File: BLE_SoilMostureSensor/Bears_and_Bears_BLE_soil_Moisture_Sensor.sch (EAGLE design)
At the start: 51 parts, among them Q1 2N3904, U2 EFR32BG13, X1 20317

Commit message: fixing antenna
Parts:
- removed FID1, FID2: FIDUCIAL"", microbuilder:FIDUCIAL""
- removed TP6: TEST-POINT3, SparkFun-Connectors:TEST-POINT3
- added R11: 4.7k, SparkFun-Resistors:4.7KOHM-0603-1/10W-1%
- added Y1: (no value), Crystal_SMD_1.2x0.6:32.768KHZ_LOW_FREQ_CRYSTAL
- L1: value L100 -> 33nH/±5%/500mA
- L2, L4: value 1.9NH -> 3.9NH
- U$3: value 38.4MHZ_CRYSTAL -> (none)
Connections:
- removed net N$52: X1.GNDDETECT
- removed net N$7: TP6.1
- removed net N$8: TP5.1
- new net GND_DETECT: R11.1, U2.PD14, X1.GNDDETECT
- new net HFXTAL_N: U$3.1, U2.HFXTAL_N
- new net HFXTAL_P: U$3.2, U2.HFXTAL_P
- new net LFXTAL_N: U2.PB14, Y1.1
- new net LFXTAL_P: U2.PB15, Y1.2
- new net N$10: U2.PF5
- new net N$11: U2.PF6
- new net N$12: U2.PF7
- new net N$16: U2.PA1
- new net N$17: U2.PA2
- new net N$18: U2.PA3
- new net N$19: U2.PA4
- new net N$2: U2.GND, U2.PAVSS, U2.RFVSS, U2.VREGVSS
- new net N$20: U2.PA5
- new net N$9: U2.PF4
- net DECOUPLE: now also U2.DECOUPLE; no longer U2.IOVDD
- net GND: now also U$3.GND, U2.2G4RF_ION
- net IOP: now also U2.2G4RF_IOP
- net PAVDD: no longer FB2.1
- net RADIO_RESET: now also U2.RESET_N
- net RFVDD: now also U2.RFVDD
- net SCL: now also U2.PC10
- net SDA: now also U2.PC11
- net SENSOR_ENABLE: now also TP5.1, U2.PD15
- net SIG: now also U2.PA0
- net SOIL_MOIST_PWR: now also U2.PD11
- net TCK: now also U2.PF0
- net TDI: now also U2.PF3
- net TDO: now also U2.PF2
- net TMS: now also U2.PF1
- net VDCDC: no longer U2.DECOUPLE
- net VDD: now also FB2.1, R11.2; no longer C4.1, C5.1, C6.1, L1.1, U2.VREGSW, U2.VREGVDD
- net VREGSW: now also U2.VREGSW
- net V_BATT: now also C4.1, C5.1, C6.1, L1.1, U2.IOVDD, U2.VREGVDD
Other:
- note removed: "VREGMCU"
- moved on the sheet: TP4, TP5

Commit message: first prototype
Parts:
- removed STANDOFF1, STANDOFF2: STAND-OFF, SparkFun-Electromechanical:STAND-OFF
- added U$4: IMAGES#JPG, images#jpg(2):IMAGES#JPG
- E1: value ANTENNA-GROUNDEDTRACE-15.2MM -> ANTENNA-GROUNDEDTRACE-25.7MM; device SparkFun-RF:ANTENNA-GROUNDEDTRACE-15.2MM -> SparkFun-RF:ANTENNA-GROUNDEDTRACE-25.7MM
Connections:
- removed net N$2: U2.GND, U2.PAVSS, U2.RFVSS, U2.VREGVSS
- net GND: now also U2.GND, U2.PAVSS, U2.RFVSS, U2.VREGVSS

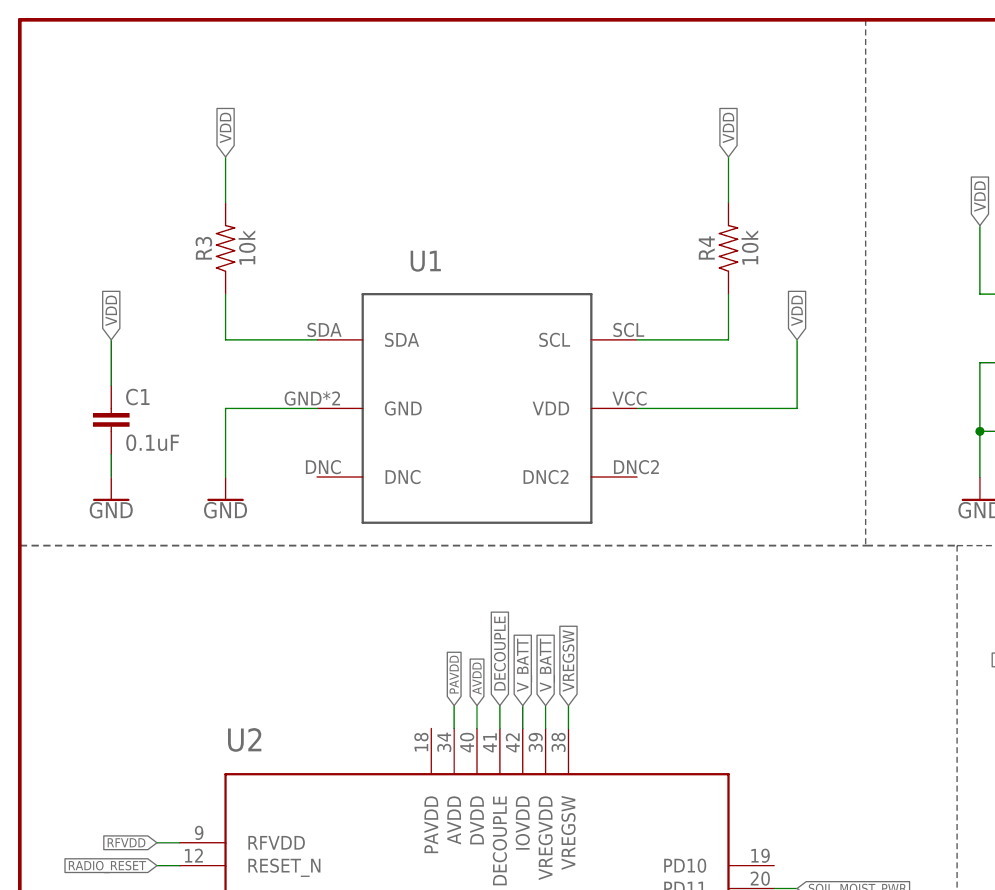
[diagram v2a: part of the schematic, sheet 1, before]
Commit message: updating sch - 12c, power
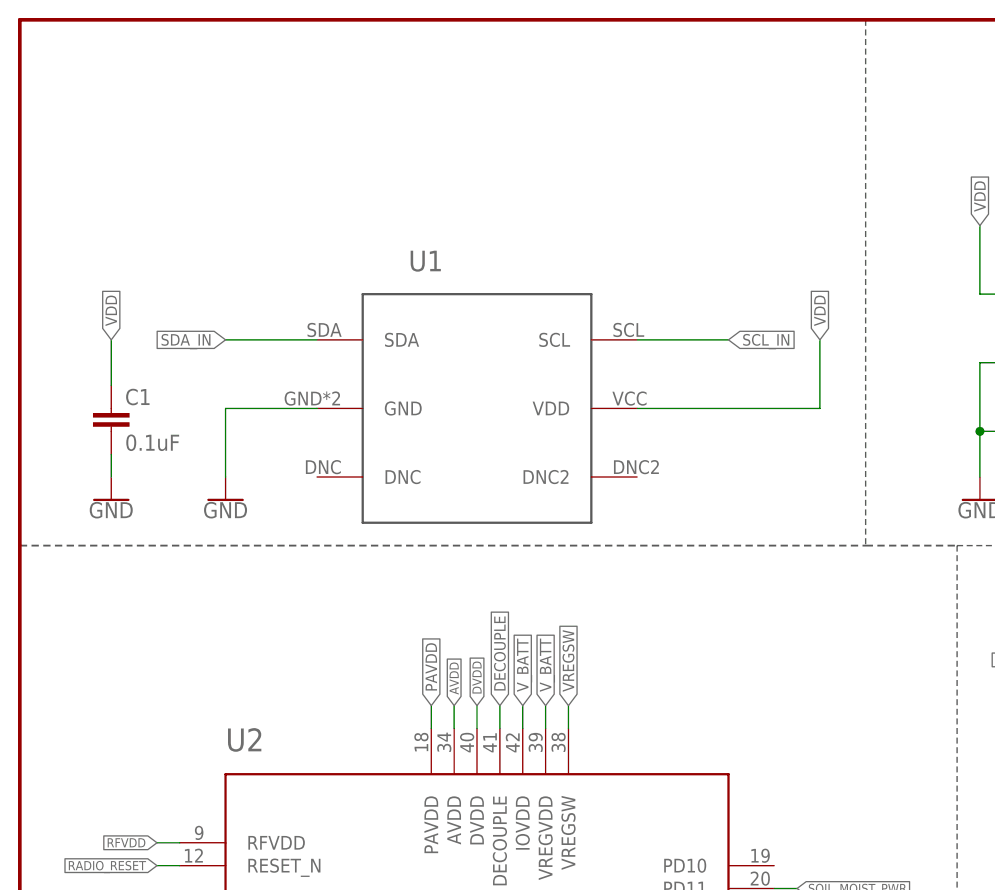
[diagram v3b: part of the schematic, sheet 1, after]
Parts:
- removed R3, R4: 10k, SparkFun-Resistors:10KOHM-0603-1/10W-1%
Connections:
- removed net N$1: R4.1, U1.SCL
- removed net N$4: R3.1, U1.SDA
- new net DVDD: U2.DVDD
- net AVDD: now also U2.AVDD; no longer U2.DVDD
- net PAVDD: now also U2.PAVDD; no longer U2.AVDD
- net SCL_IN: now also U1.SCL
- net SDA_IN: now also U1.SDA
- net VDD: no longer R3.2, R4.2
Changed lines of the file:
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@@
 <part name="U1" library="Si7021_A20" deviceset="SI7021_TEMP_HUMIDTY" device=""/>
 <part name="C1" library="SparkFun-Capacitors" deviceset="0.1UF" device="-0603-25V-(+80/-20%)" value="0.1uF"/>
-<part name="R3" library="SparkFun-Resistors" deviceset="10KOHM" device="-0603-1/10W-1%" value="10k"/>
-<part name="R4" library="SparkFun-Resistors" deviceset="10KOHM" device="-0603-1/10W-1%" value="10k"/>
 <part name="GND2" library="SparkFun-PowerSymbols" deviceset="GND" device=""/>
 <part name="GND3" library="SparkFun-PowerSymbols" deviceset="GND" device=""/>
@@
 <instance part="U1" gate="G$1" x="38.1" y="129.54"/>
 <instance part="C1" gate="G$1" x="10.16" y="139.7"/>
-<instance part="R3" gate="G$1" x="22.86" y="160.02" rot="R90"/>
-<instance part="R4" gate="G$1" x="78.74" y="160.02" rot="R90"/>
 <instance part="GND2" gate="1" x="22.86" y="132.08"/>
 <instance part="GND3" gate="1" x="10.16" y="132.08"/>
@@
 </segment>
 </net>
-<net name="N$1" class="0">
-<segment>
-<pinref part="U1" gate="G$1" pin="SCL"/>
-<wire x1="68.58" y1="149.86" x2="78.74" y2="149.86" width="0.1524" layer="91"/>
-<pinref part="R4" gate="G$1" pin="1"/>
-<wire x1="78.74" y1="149.86" x2="78.74" y2="154.94" width="0.1524" layer="91"/>
-</segment>
-</net>
-<net name="N$4" class="0">
-<segment>
-<pinref part="U1" gate="G$1" pin="SDA"/>
-<wire x1="33.02" y1="149.86" x2="22.86" y2="149.86" width="0.1524" layer="91"/>
-<pinref part="R3" gate="G$1" pin="1"/>
-<wire x1="22.86" y1="149.86" x2="22.86" y2="154.94" width="0.1524" layer="91"/>
-</segment>
-</net>
 <net name="SCL_IN" class="0">
 <segment>
@@
 <label x="154.94" y="68.58" size="1.27" layer="95" rot="R180" xref="yes"/>
 </segment>
+<segment>
+<pinref part="U1" gate="G$1" pin="SCL"/>
+<wire x1="68.58" y1="149.86" x2="78.74" y2="149.86" width="0.1524" layer="91"/>
+<label x="78.74" y="149.86" size="1.27" layer="95" xref="yes"/>
+</segment>
 </net>
 <net name="SCL" class="0">
@@
 </segment>
 <segment>
-<pinref part="R3" gate="G$1" pin="2"/>
-<wire x1="22.86" y1="170.18" x2="22.86" y2="165.1" width="0.1524" layer="91"/>
-<label x="22.86" y="170.18" size="1.27" layer="95" font="vector" rot="R90" xref="yes"/>
-</segment>
-<segment>
-<pinref part="R4" gate="G$1" pin="2"/>
-<wire x1="78.74" y1="170.18" x2="78.74" y2="165.1" width="0.1524" layer="91"/>
-<label x="78.74" y="170.18" size="1.27" layer="95" font="vector" rot="R90" xref="yes"/>
-</segment>
-<segment>
 <pinref part="U1" gate="G$1" pin="VDD"/>
-<wire x1="68.58" y1="142.24" x2="86.36" y2="142.24" width="0.1524" layer="91"/>
-<wire x1="86.36" y1="142.24" x2="86.36" y2="149.86" width="0.1524" layer="91"/>
-<label x="86.36" y="149.86" size="1.27" layer="95" font="vector" rot="R90" xref="yes"/>
+<wire x1="68.58" y1="142.24" x2="88.9" y2="142.24" width="0.1524" layer="91"/>
+<wire x1="88.9" y1="142.24" x2="88.9" y2="149.86" width="0.1524" layer="91"/>
+<label x="88.9" y="149.86" size="1.27" layer="95" font="vector" rot="R90" xref="yes"/>
 </segment>
 <segment>
@@
 <wire x1="157.48" y1="53.34" x2="154.94" y2="53.34" width="0.1524" layer="91"/>
 <label x="154.94" y="53.34" size="1.27" layer="95" rot="R180" xref="yes"/>
+</segment>
+<segment>
+<pinref part="U1" gate="G$1" pin="SDA"/>
+<wire x1="33.02" y1="149.86" x2="22.86" y2="149.86" width="0.1524" layer="91"/>
+<label x="22.86" y="149.86" size="1.27" layer="95" rot="R180" xref="yes"/>
 </segment>
 </net>
@@
 </segment>
 <segment>
-<wire x1="50.8" y1="106.68" x2="50.8" y2="109.22" width="0.1524" layer="91"/>
-<label x="50.8" y="109.22" size="1.016" layer="95" rot="R90" xref="yes"/>
-<pinref part="U2" gate="G$1" pin="DVDD"/>
+<wire x1="48.26" y1="106.68" x2="48.26" y2="109.22" width="0.1524" layer="91"/>
+<label x="48.26" y="109.22" size="1.016" layer="95" rot="R90" xref="yes"/>
+<pinref part="U2" gate="G$1" pin="AVDD"/>
 </segment>
 </net>
@@
 </segment>
 <segment>
-<wire x1="48.26" y1="106.68" x2="48.26" y2="109.22" width="0.1524" layer="91"/>
-<label x="48.26" y="109.22" size="1.016" layer="95" rot="R90" xref="yes"/>
-<pinref part="U2" gate="G$1" pin="AVDD"/>
+<pinref part="U2" gate="G$1" pin="PAVDD"/>
+<wire x1="45.72" y1="106.68" x2="45.72" y2="109.22" width="0.1524" layer="91"/>
+<label x="45.72" y="109.22" size="1.27" layer="95" rot="R90" xref="yes"/>
 </segment>
 </net>
@@
 <pinref part="U2" gate="G$1" pin="PD14"/>
 <wire x1="83.82" y1="81.28" x2="86.36" y2="81.28" width="0.1524" layer="91"/>
-<label x="86.36" y="81.28" size="1.27" layer="95" xref="yes"/>
+<label x="86.36" y="81.28" size="1.27" layer="95" font="vector" xref="yes"/>
 </segment>
 </net>
@@
 <pinref part="U2" gate="G$1" pin="PB14"/>
 <wire x1="83.82" y1="60.96" x2="88.9" y2="60.96" width="0.1524" layer="91"/>
-<label x="88.9" y="60.96" size="1.27" layer="95" xref="yes"/>
+<label x="88.9" y="60.96" size="1.27" layer="95" font="vector" xref="yes"/>
 </segment>
 <segment>
@@
 </segment>
 </net>
+<net name="DVDD" class="0">
+<segment>
+<wire x1="50.8" y1="106.68" x2="50.8" y2="109.22" width="0.1524" layer="91"/>
+<label x="50.8" y="109.22" size="1.016" layer="95" rot="R90" xref="yes"/>
+<pinref part="U2" gate="G$1" pin="DVDD"/>
+</segment>
+</net>

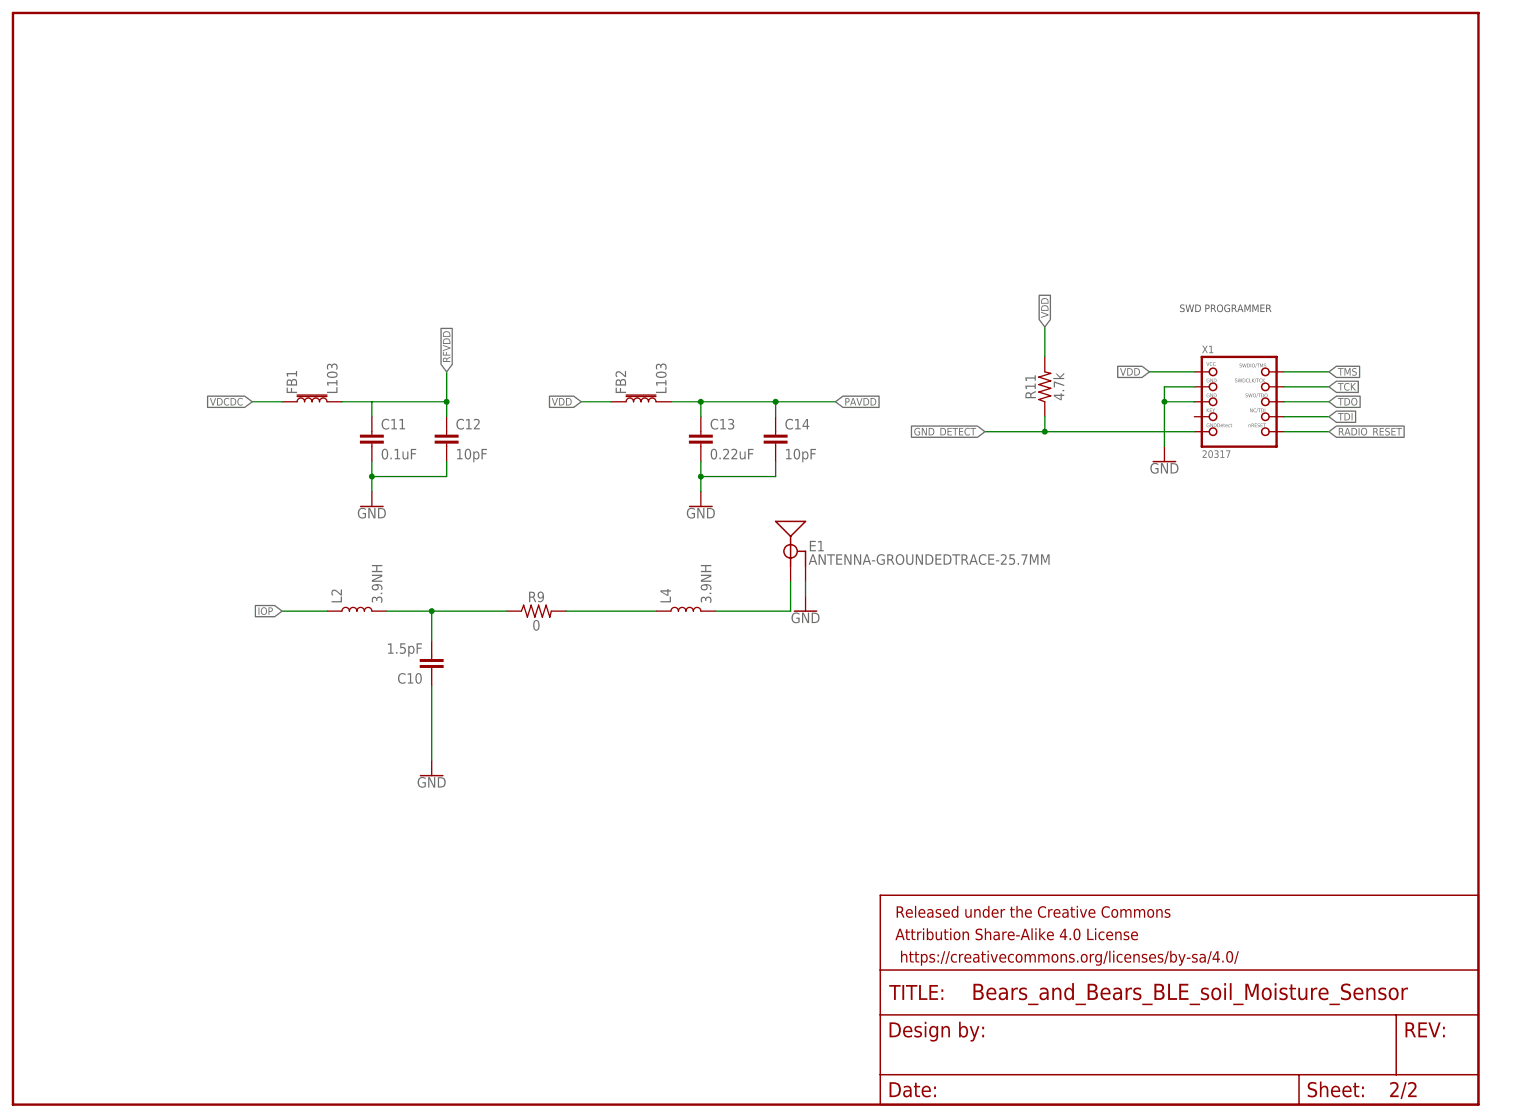
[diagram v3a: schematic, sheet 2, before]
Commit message: Make required changes:
- Rotate temp sensor and reroute
- Route AVDD to MCU
- Route PAVDD to MCU
- Change SWD jack to POGO type
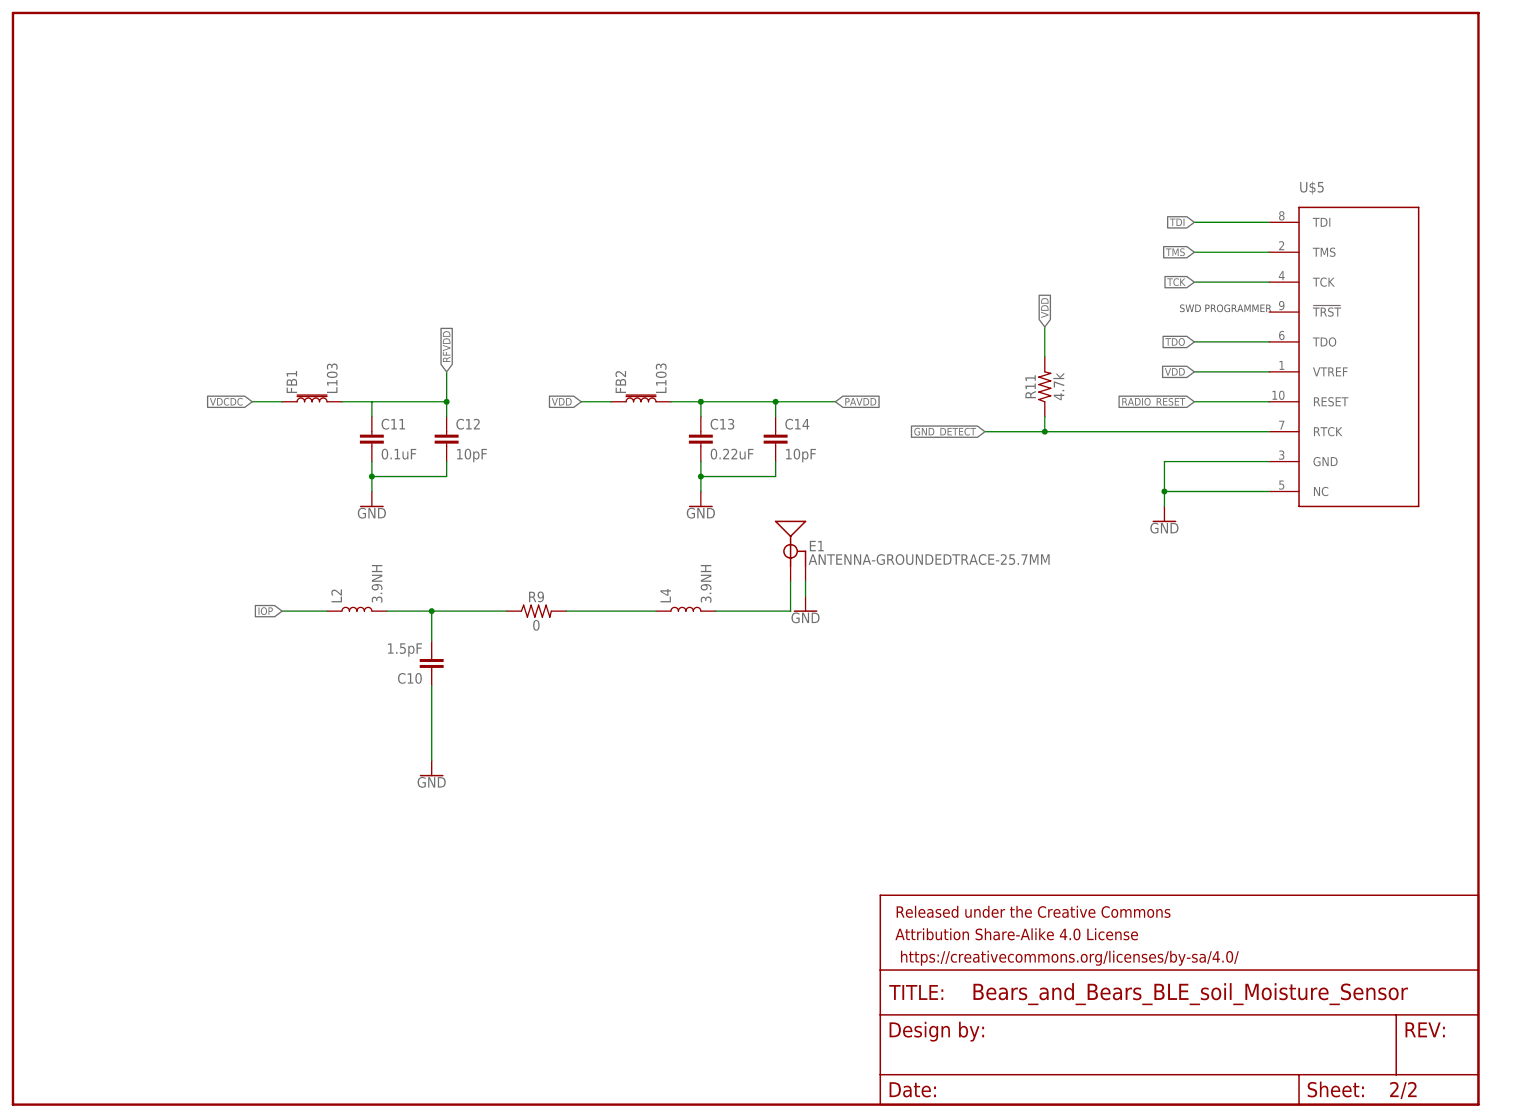
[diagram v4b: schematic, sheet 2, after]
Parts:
- removed X1: 20317, microbuilder:JTAG-CORTEXBOXPOSTS
- added U$5: TC2050-MCP-NL, TC2050:TC2050-MCP-NL
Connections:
- net GND: now also U$5.GND, U$5.NC; no longer X1.GND@1, X1.GND@2
- net GND_DETECT: now also U$5.RTCK; no longer X1.GNDDETECT
- net RADIO_RESET: now also U$5.RESET; no longer X1.NRESET
- net TCK: now also U$5.TCK; no longer X1.SWDCLK
- net TDI: now also U$5.TDI; no longer X1.TDI
- net TDO: now also U$5.TDO; no longer X1.SWO
- net TMS: now also U$5.TMS; no longer X1.SWDIO
- net VDD: now also U$5.VTREF; no longer X1.VCC

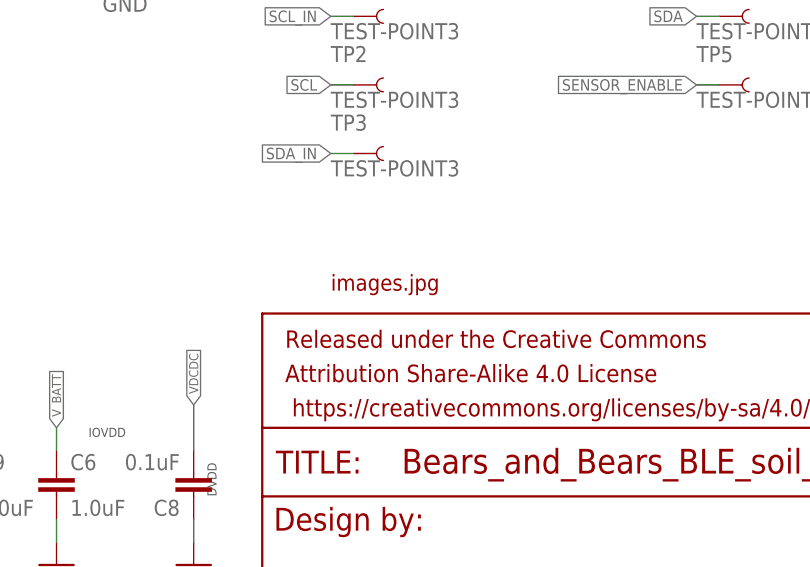
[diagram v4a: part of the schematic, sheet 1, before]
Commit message: 1. MDE BOARD SMALLER, RE DID LAYOUT, DELETED SILK. TO DO: REPLACE SILK, FINISH ROUTING, POLYGON PROCESSING, IN DEPTH DESIGN REVIEW, REVIEW nrf ANTENNA REQUIREMENT AND LAYOUT SUGGESTIONS
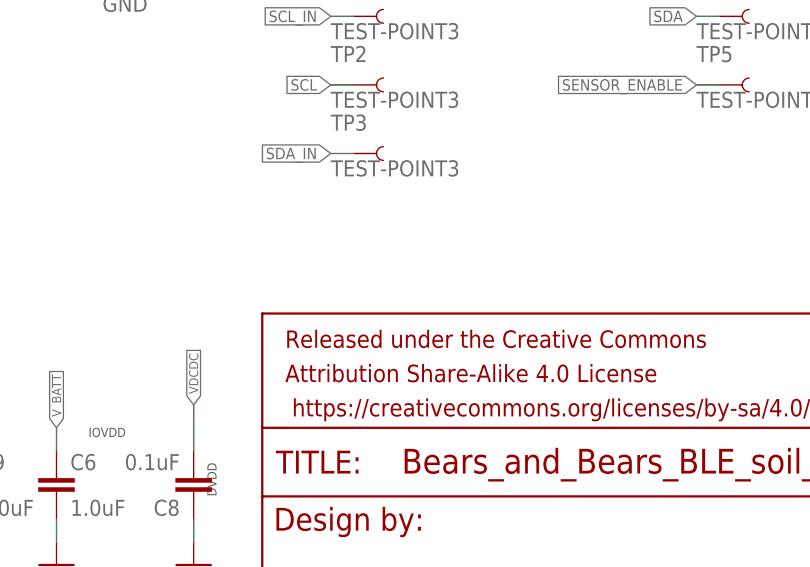
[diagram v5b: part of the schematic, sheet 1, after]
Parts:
- removed U$4: IMAGES#JPG, images#jpg(2):IMAGES#JPG
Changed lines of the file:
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@@
 <?xml version="1.0" encoding="utf-8"?>
 <!DOCTYPE eagle SYSTEM "eagle.dtd">
-<eagle version="9.2.2">
+<eagle version="9.1.0">
 <drawing>
 <settings>
@@
 <part name="GND22" library="SparkFun-PowerSymbols" deviceset="GND" device=""/>
 <part name="Y1" library="Crystal_SMD_1.2x0.6" deviceset="32.768KHZ_LOW_FREQ_CRYSTAL" device=""/>
-<part name="U$4" library="images#jpg(2)" deviceset="IMAGES#JPG" device=""/>
 <part name="U$5" library="TC2050" deviceset="TC2050" device="-MCP-NL"/>
 </parts>
@@
 <attribute name="VALUE" x="22.86" y="8.128" size="1.778" layer="96" font="vector" align="top-center"/>
 </instance>
-<instance part="U$4" gate="G$1" x="157.48" y="38.1" smashed="yes"/>
 </instances>
 <busses>
